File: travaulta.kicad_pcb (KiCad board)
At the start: 4 copper layers, 209.7 x 76.4 mm, 105 parts, among them SW1 EC_SW, SW10 EC_SW, SW11 EC_SW, SW12 EC_SW, SW13 EC_SW, SW14 EC_SW, SW15 EC_SW, SW16 EC_SW, SW17 EC_SW, SW18 EC_SW, SW19 EC_SW, SW2 EC_SW, SW20 EC_SW, SW21 EC_SW, SW22 EC_SW, SW23 EC_SW, SW24 EC_SW, SW25 EC_SW, SW26 EC_SW, SW27 EC_SW, SW28 EC_SW, SW29 EC_SW, SW3 EC_SW, SW30 EC_SW, SW31 EC_SW, SW32 EC_SW, SW33 EC_SW, SW34 EC_SW, SW35 EC_SW, SW36 EC_SW, SW37 EC_SW, SW38 BOOT0, SW4 EC_SW, SW5 EC_SW, SW6 EC_SW, SW7 EC_SW, SW8 EC_SW, SW9 EC_SW, U1 STM32F401CBUx, U2 XC6206PxxxMR, U3 74HC4051, U4 74HC4051, U5 OPA350, Y1 8 MHz

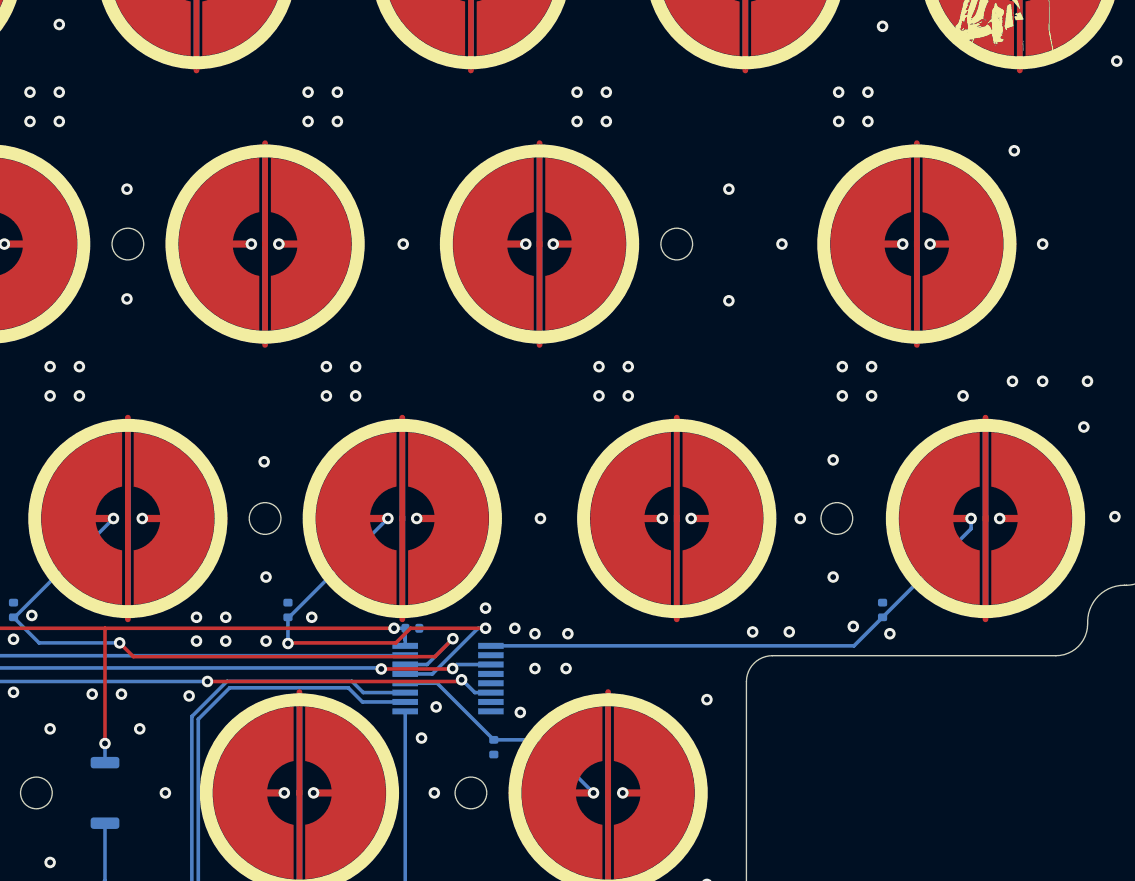
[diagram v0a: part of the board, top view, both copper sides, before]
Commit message: rerouting matrix to fix error
shifting around a bunch of switches, ending up with hopefully functional but not pretty routing
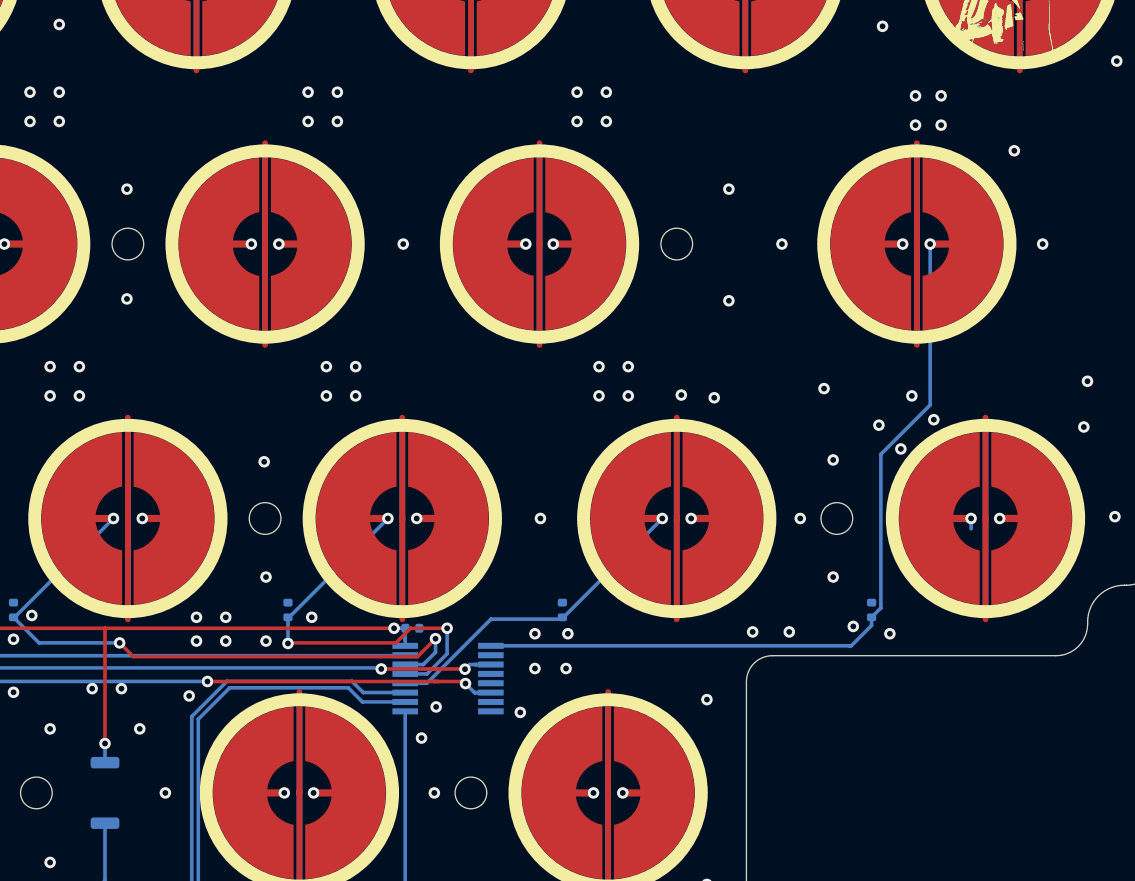
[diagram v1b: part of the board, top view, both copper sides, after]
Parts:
- moved R14 10.6 mm to (212.7, 101.6), turned to 90 degrees
- moved R16 0.76 mm to (234.2, 101.6)
- turned SW21 to 0 degrees
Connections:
- SW11 pad 1: ROW0 -> ROW1
- SW21 pad 1: ROW1 -> ROW2
- SW31 pad 1: ROW2 -> ROW3
- SW31 pad 2: COL9 -> COL8
- SW36 pad 2: COL7 -> COL6
- SW37 pad 2: COL8 -> COL7
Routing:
- net ROW3: track 220.8 -> 269.0 mm, vias 8 -> 9
- net ROW0: track 373.4 -> 342.2 mm, vias 13 -> 12
- net COL6: track 91.5 -> 120.7 mm, vias 5 -> 6
- net COL9: track 129.8 -> 108.6 mm, vias 4 -> 3
- net COL8: track 85.3 -> 101.9 mm
- net ROW1: track 348.8 -> 362.6 mm
- net ROW2: track 323.2 -> 312.7 mm
- net COL7: track 104.2 -> 106.9 mm
- net APLEX_EN_PIN_1: track 73.7 -> 75.1 mm, vias 4 -> 6
- net APLEX_OUT_PIN_0: track 138.0 -> 138.8 mm
- net GND: vias 275 -> 271

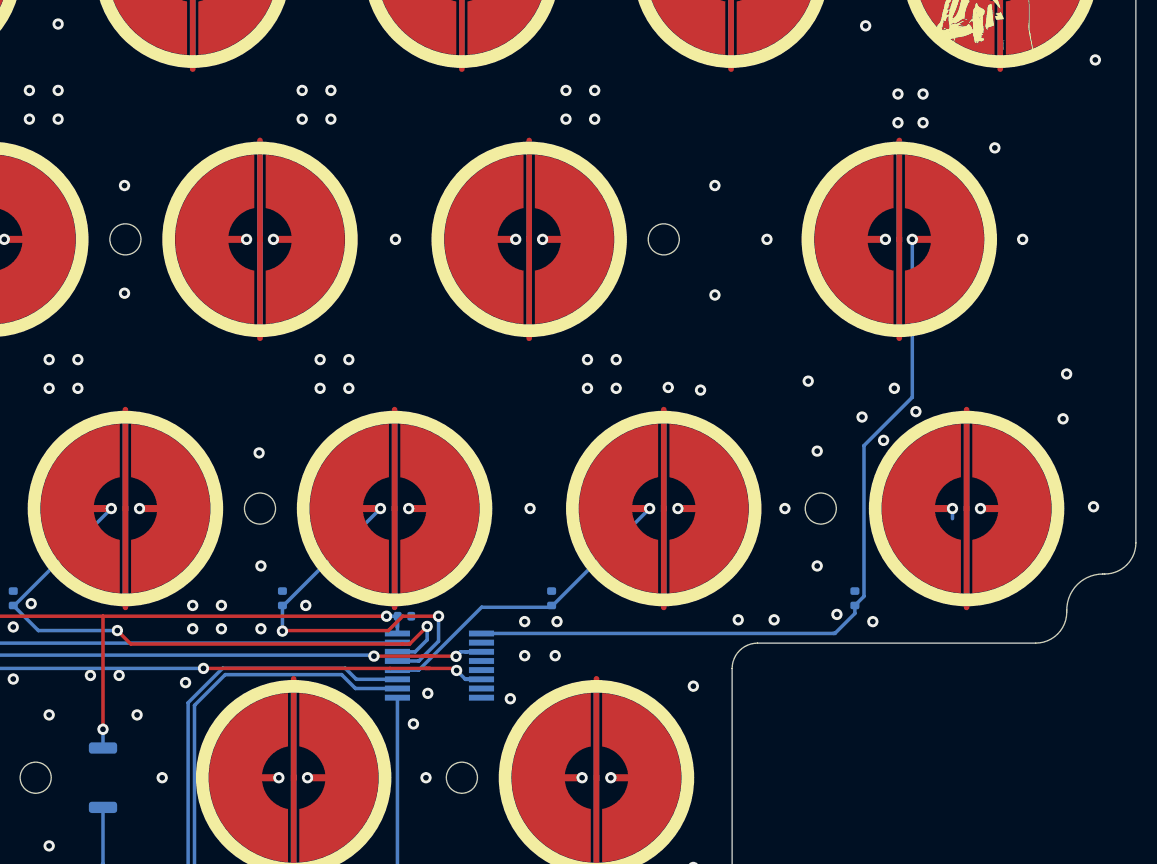
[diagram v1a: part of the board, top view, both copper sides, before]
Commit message: one pin matrix fix
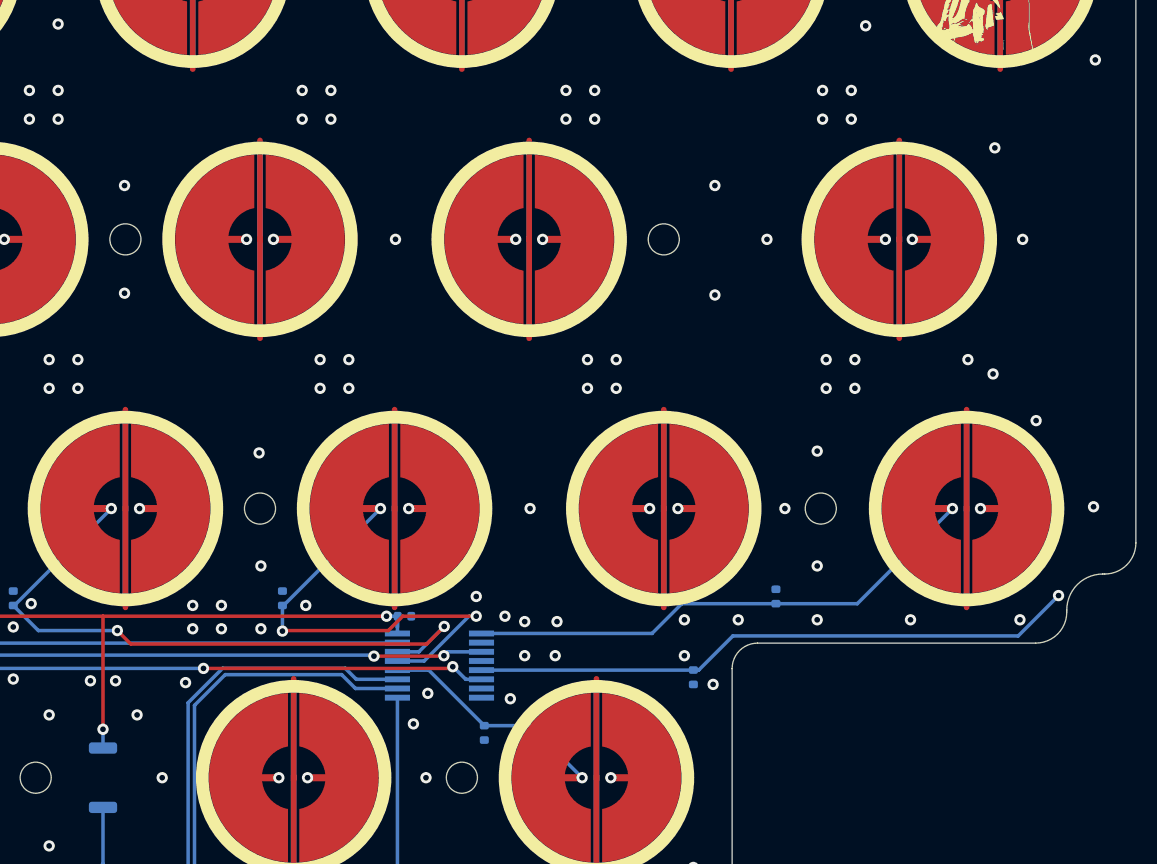
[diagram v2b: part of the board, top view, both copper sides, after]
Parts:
- added R5: 100k, Resistor_SMD:R_0402_1005Metric, B.Cu at (222.8, 107.2)
- moved R14 10.6 mm to (208.0, 111.1), turned to -90 degrees
- moved R16 5.59 mm to (228.6, 101.5)
- turned SW21 to 180 degrees
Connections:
- SW11 pad 1: ROW1 -> ROW0
- SW11 pad 2: COL9 -> COL10
- SW11 pad 3: GND -> unconnected-(SW11-SG-Pad3)
- SW21 pad 1: ROW2 -> ROW1
- SW31 pad 1: ROW3 -> ROW2
- SW31 pad 2: COL8 -> COL9
- SW36 pad 2: COL6 -> COL7
- SW37 pad 2: COL7 -> COL8
- U3 pad 5: GND -> COL10
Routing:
- net COL10: track 0.00 -> 89.5 mm, vias 0 -> 2
- net ROW3: track 269.0 -> 220.8 mm, vias 9 -> 8
- net ROW0: track 342.2 -> 373.4 mm, vias 12 -> 13
- net COL6: track 120.7 -> 91.5 mm, vias 6 -> 5
- net COL9: track 108.6 -> 84.0 mm
- net COL8: track 101.9 -> 85.3 mm
- net ROW1: track 362.6 -> 348.8 mm
- net ROW2: track 312.7 -> 323.2 mm
- net COL7: track 106.9 -> 104.2 mm
- net APLEX_EN_PIN_1: track 75.1 -> 73.7 mm, vias 6 -> 4
- net APLEX_OUT_PIN_0: track 138.8 -> 138.0 mm
- net GND: vias 271 -> 275

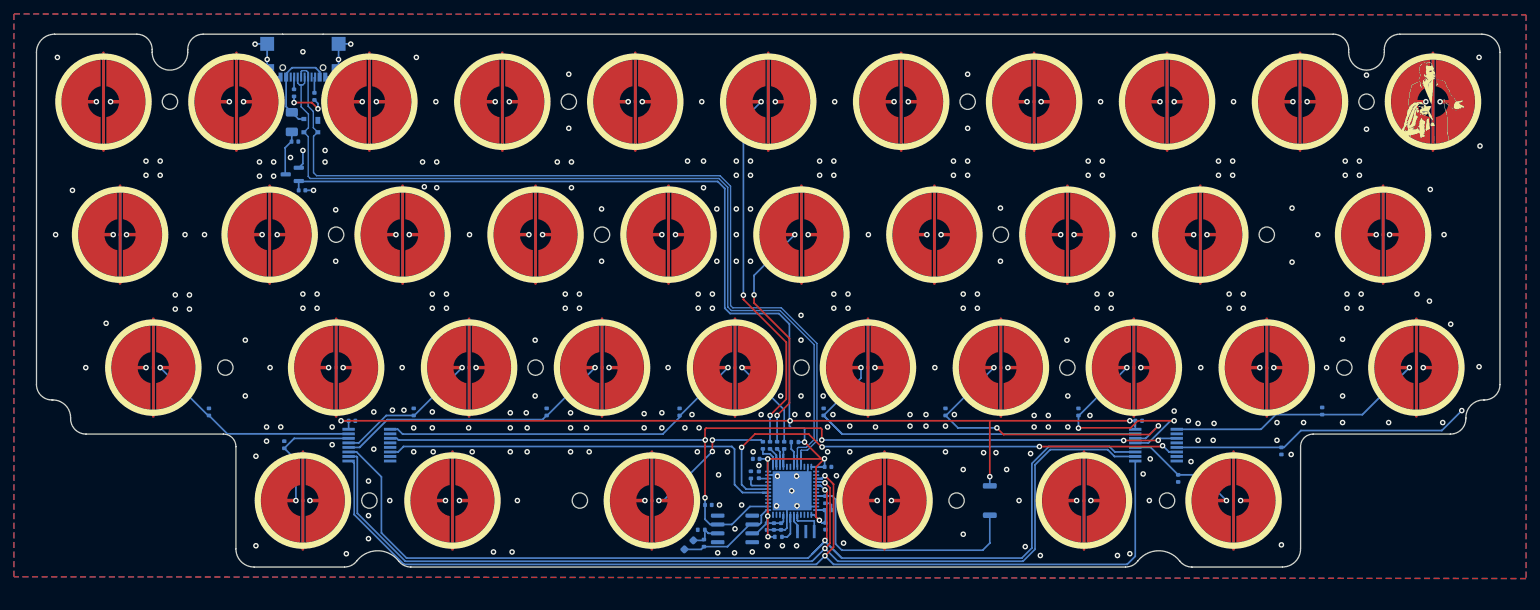
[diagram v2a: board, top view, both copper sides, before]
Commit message: edited preliminary firmware, small routing cleanups
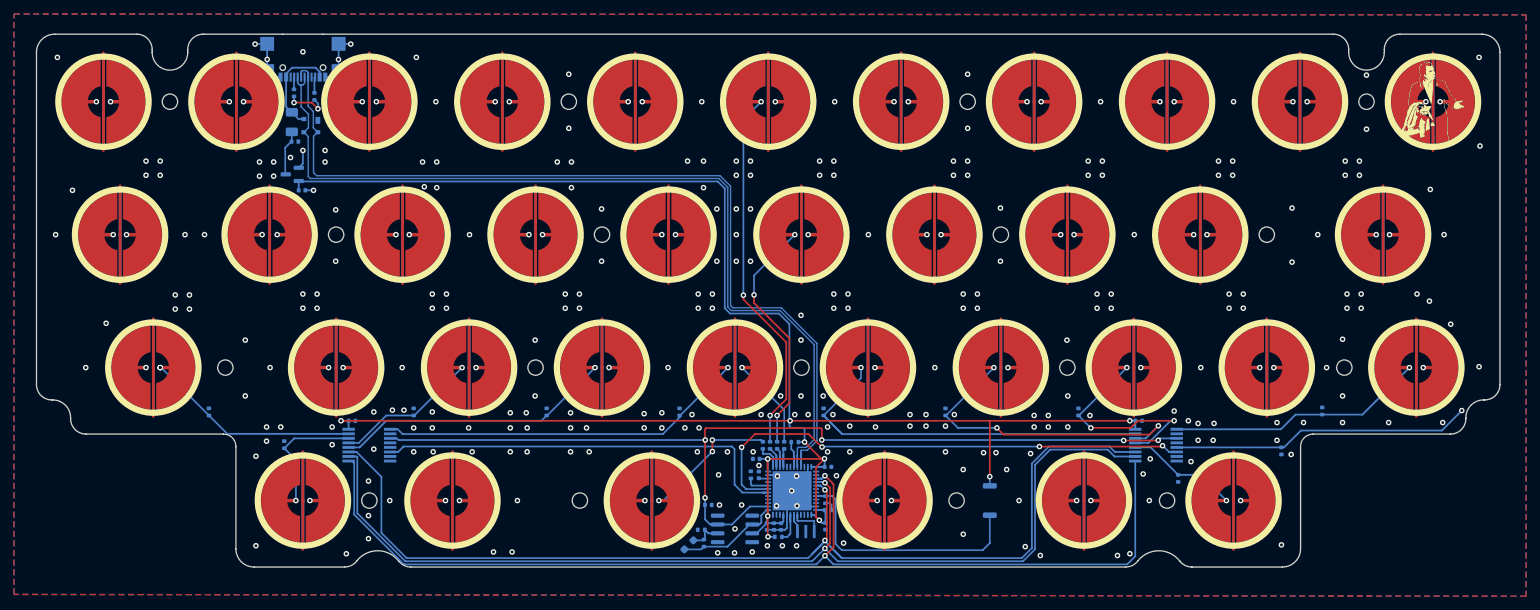
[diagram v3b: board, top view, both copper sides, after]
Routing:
- net COL7: track 104.2 -> 103.1 mm
- net COL0: vias 3 -> 4
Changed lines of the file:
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@@
   (segment (start 146.742 111.127) (end 146.742 112.014) (width 0.25) (layer "B.Cu") (net 13))
+  (via (at 62.103 95.25) (size 0.8) (drill 0.4) (layers "F.Cu" "B.Cu") (net 14))
   (via (at 62.103 95.25) (size 0.8) (drill 0.4) (layers "F.Cu" "B.Cu") (net 14))
   (via (at 54.991 57.15) (size 0.8) (drill 0.4) (layers "F.Cu" "B.Cu") (net 14))
@@
   (segment (start 61.087 63.246) (end 61.087 72.39) (width 0.5) (layer "In2.Cu") (net 14))
   (segment (start 69.088 102.11) (end 71.707651 104.729651) (width 0.25) (layer "B.Cu") (net 14))
-  (segment (start 68.963 102.11) (end 62.103 95.25) (width 0.25) (layer "B.Cu") (net 14))
   (segment (start 71.707651 104.729651) (end 71.74099 104.73944) (width 0.25) (layer "B.Cu") (net 14))
-  (segment (start 69.088 102.11) (end 68.963 102.11) (width 0.25) (layer "B.Cu") (net 14))
+  (segment (start 62.228 95.25) (end 62.103 95.25) (width 0.25) (layer "B.Cu") (net 14))
+  (segment (start 69.088 102.11) (end 62.228 95.25) (width 0.25) (layer "B.Cu") (net 14))
   (segment (start 71.74099 104.73944) (end 89.10066 104.73944) (width 0.25) (layer "B.Cu") (net 14))
   (via (at 74.041 57.15) (size 0.8) (drill 0.4) (layers "F.Cu" "B.Cu") (net 15))
@@
   (segment (start 112.125 57.15) (end 120.015 65.04) (width 0.5) (layer "In2.Cu") (net 17))
   (segment (start 120.015 73.0725) (end 116.8875 76.2) (width 0.5) (layer "In2.Cu") (net 17))
+  (segment (start 94.488 102.87) (end 116.715 102.87) (width 0.25) (layer "B.Cu") (net 17))
+  (segment (start 90.67292 106.68508) (end 94.488 102.87) (width 0.25) (layer "B.Cu") (net 17))
+  (segment (start 117.5525 102.11) (end 124.4125 95.25) (width 0.25) (layer "B.Cu") (net 17))
   (segment (start 89.10066 106.68508) (end 90.67292 106.68508) (width 0.25) (layer "B.Cu") (net 17))
-  (segment (start 94.653 102.705) (end 116.88 102.705) (width 0.25) (layer "B.Cu") (net 17))
-  (segment (start 117.5525 102.11) (end 124.4125 95.25) (width 0.25) (layer "B.Cu") (net 17))
-  (segment (start 116.88 102.705) (end 117.475 102.11) (width 0.25) (layer "B.Cu") (net 17))
   (segment (start 117.475 102.11) (end 117.5525 102.11) (width 0.25) (layer "B.Cu") (net 17))
-  (segment (start 90.67292 106.68508) (end 94.653 102.705) (width 0.25) (layer "B.Cu") (net 17))
+  (segment (start 116.715 102.87) (end 117.475 102.11) (width 0.25) (layer "B.Cu") (net 17))
   (via (at 143.4625 95.25) (size 0.8) (drill 0.4) (layers "F.Cu" "B.Cu") (net 18))
   (via (at 135.9375 76.2) (size 0.8) (drill 0.4) (layers "F.Cu" "B.Cu") (net 18))
@@
   (segment (start 201.81316 105.38968) (end 203.329416 105.38968) (width 0.25) (layer "B.Cu") (net 20))
   (segment (start 181.991 103.886) (end 176.401 103.886) (width 0.25) (layer "B.Cu") (net 20))
-  (segment (start 201.168 103.886) (end 193.7145 103.886) (width 0.25) (layer "F.Cu") (net 21))
+  (segment (start 201.168 103.886) (end 195.453 103.886) (width 0.25) (layer "F.Cu") (net 21))
   (segment (start 207.391 102.87) (end 202.184 102.87) (width 0.25) (layer "F.Cu") (net 21))
-  (segment (start 193.7145 103.886) (end 193.675 103.9255) (width 0.25) (layer "F.Cu") (net 21))
   (segment (start 202.184 102.87) (end 201.168 103.886) (width 0.25) (layer "F.Cu") (net 21))
   (via (at 188.325 57.15) (size 0.8) (drill 0.4) (layers "F.Cu" "B.Cu") (net 21))
@@
   (via (at 207.391 102.87) (size 0.8) (drill 0.4) (layers "F.Cu" "B.Cu") (net 21))
   (via (at 193.421 114.3) (size 0.8) (drill 0.4) (layers "F.Cu" "B.Cu") (net 21))
-  (via (at 193.675 103.9255) (size 0.8) (drill 0.4) (layers "F.Cu" "B.Cu") (net 21))
+  (via (at 195.453 103.886) (size 0.8) (drill 0.4) (layers "F.Cu" "B.Cu") (net 21))
   (via (at 193.04 76.2) (size 0.8) (drill 0.4) (layers "F.Cu" "B.Cu") (net 21))
   (segment (start 188.325 57.15) (end 196.088 64.913) (width 0.5) (layer "In2.Cu") (net 21))
@@
   (segment (start 193.675 102.11) (end 193.7525 102.11) (width 0.25) (layer "B.Cu") (net 21))
   (segment (start 203.703775 106.03992) (end 206.873694 102.87) (width 0.25) (layer "B.Cu") (net 21))
+  (segment (start 193.677 102.11) (end 195.453 103.886) (width 0.25) (layer "B.Cu") (net 21))
   (segment (start 201.81316 106.03992) (end 203.703775 106.03992) (width 0.25) (layer "B.Cu") (net 21))
   (segment (start 193.7525 102.11) (end 200.6125 95.25) (width 0.25) (layer "B.Cu") (net 21))
-  (segment (start 193.675 102.11) (end 193.675 103.9255) (width 0.25) (layer "B.Cu") (net 21))
   (segment (start 206.873694 102.87) (end 207.391 102.87) (width 0.25) (layer "B.Cu") (net 21))
+  (segment (start 193.675 102.11) (end 193.677 102.11) (width 0.25) (layer "B.Cu") (net 21))
   (via (at 207.391 57.15) (size 0.8) (drill 0.4) (layers "F.Cu" "B.Cu") (net 22))
   (via (at 214.884 114.3) (size 0.8) (drill 0.4) (layers "F.Cu" "B.Cu") (net 22))
@@
   (segment (start 226.441 57.15) (end 232.918 63.627) (width 0.5) (layer "In2.Cu") (net 23))
   (segment (start 233.172 87.327) (end 233.172 79.375) (width 0.5) (layer "In2.Cu") (net 23))
-  (segment (start 221.9432 101.983) (end 219.837 104.0892) (width 0.25) (layer "B.Cu") (net 23))
-  (segment (start 207.76184 104.0892) (end 219.837 104.0892) (width 0.25) (layer "B.Cu") (net 23))
-  (segment (start 228.6 101.983) (end 221.9432 101.983) (width 0.25) (layer "B.Cu") (net 23))
+  (segment (start 224.79 101.983) (end 228.6 101.983) (width 0.25) (layer "B.Cu") (net 23))
+  (segment (start 207.76184 104.0892) (end 222.6838 104.0892) (width 0.25) (layer "B.Cu") (net 23))
+  (segment (start 222.6838 104.0892) (end 224.79 101.983) (width 0.25) (layer "B.Cu") (net 23))
   (segment (start 241.095 95.25) (end 234.362 101.983) (width 0.25) (layer "B.Cu") (net 23))
   (segment (start 234.362 101.983) (end 228.6 101.983) (width 0.25) (layer "B.Cu") (net 23))
@@
       (pts
         (xy 257.81 44.704)
-        (xy 257.81 125.476)
-        (xy 41.148 125.222)
+        (xy 257.81 128.006622)
+        (xy 41.148 127.752622)
         (xy 41.148 44.577)
       )
